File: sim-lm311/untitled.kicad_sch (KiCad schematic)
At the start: 6 parts, among them Q1 NMOS, Q2 NMOS, U4 L7805

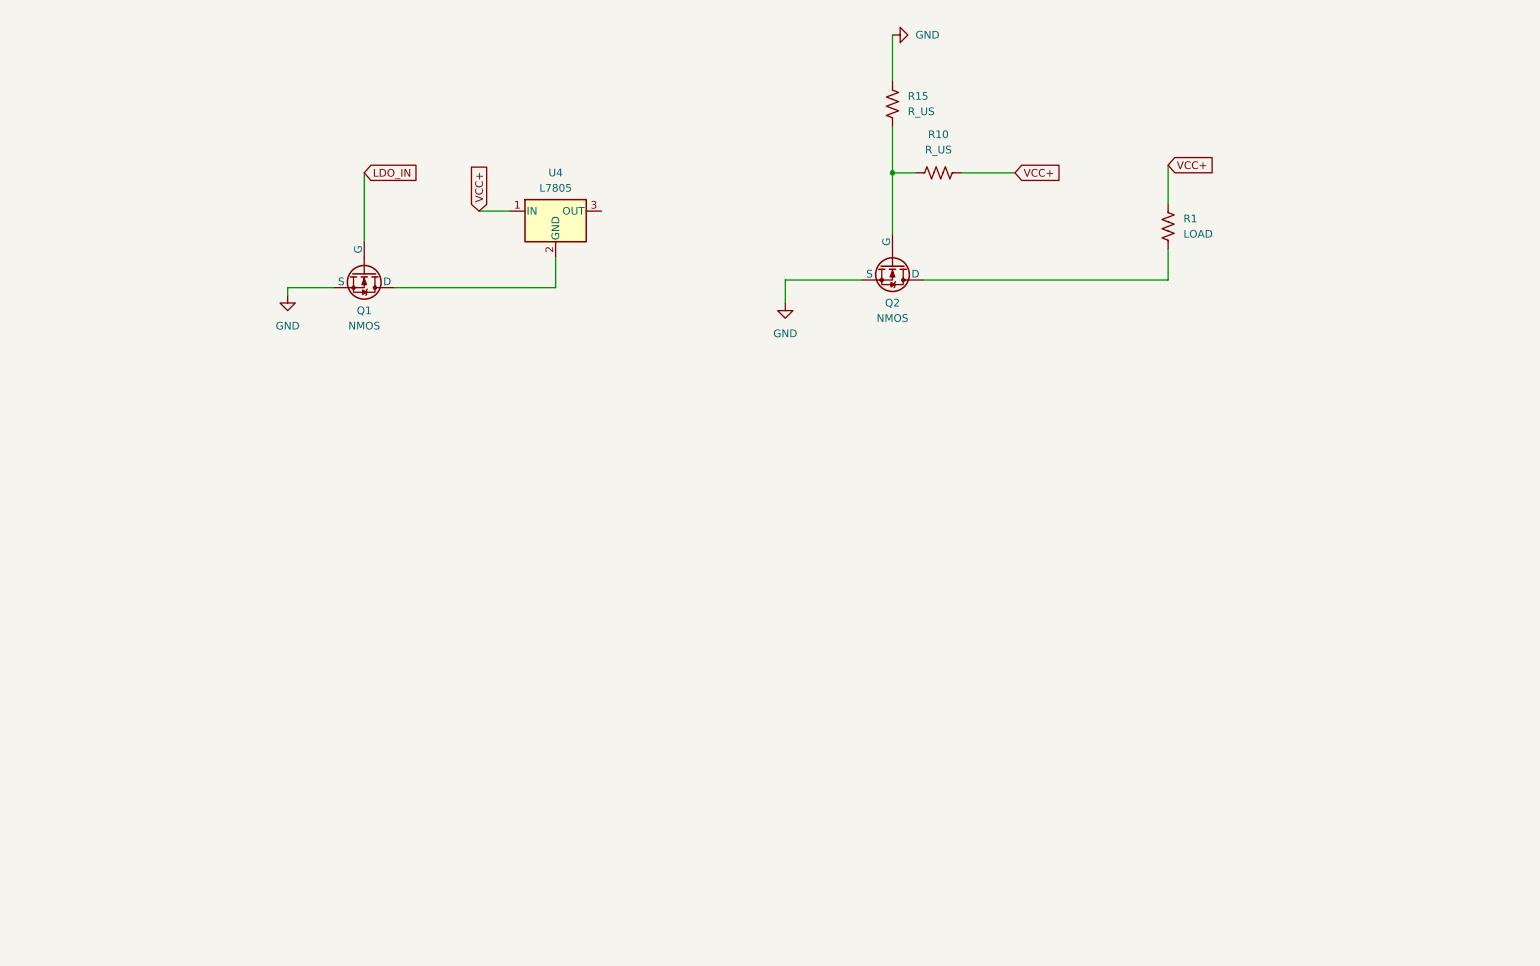
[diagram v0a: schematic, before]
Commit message: updated prototyping subcircuit under lm311
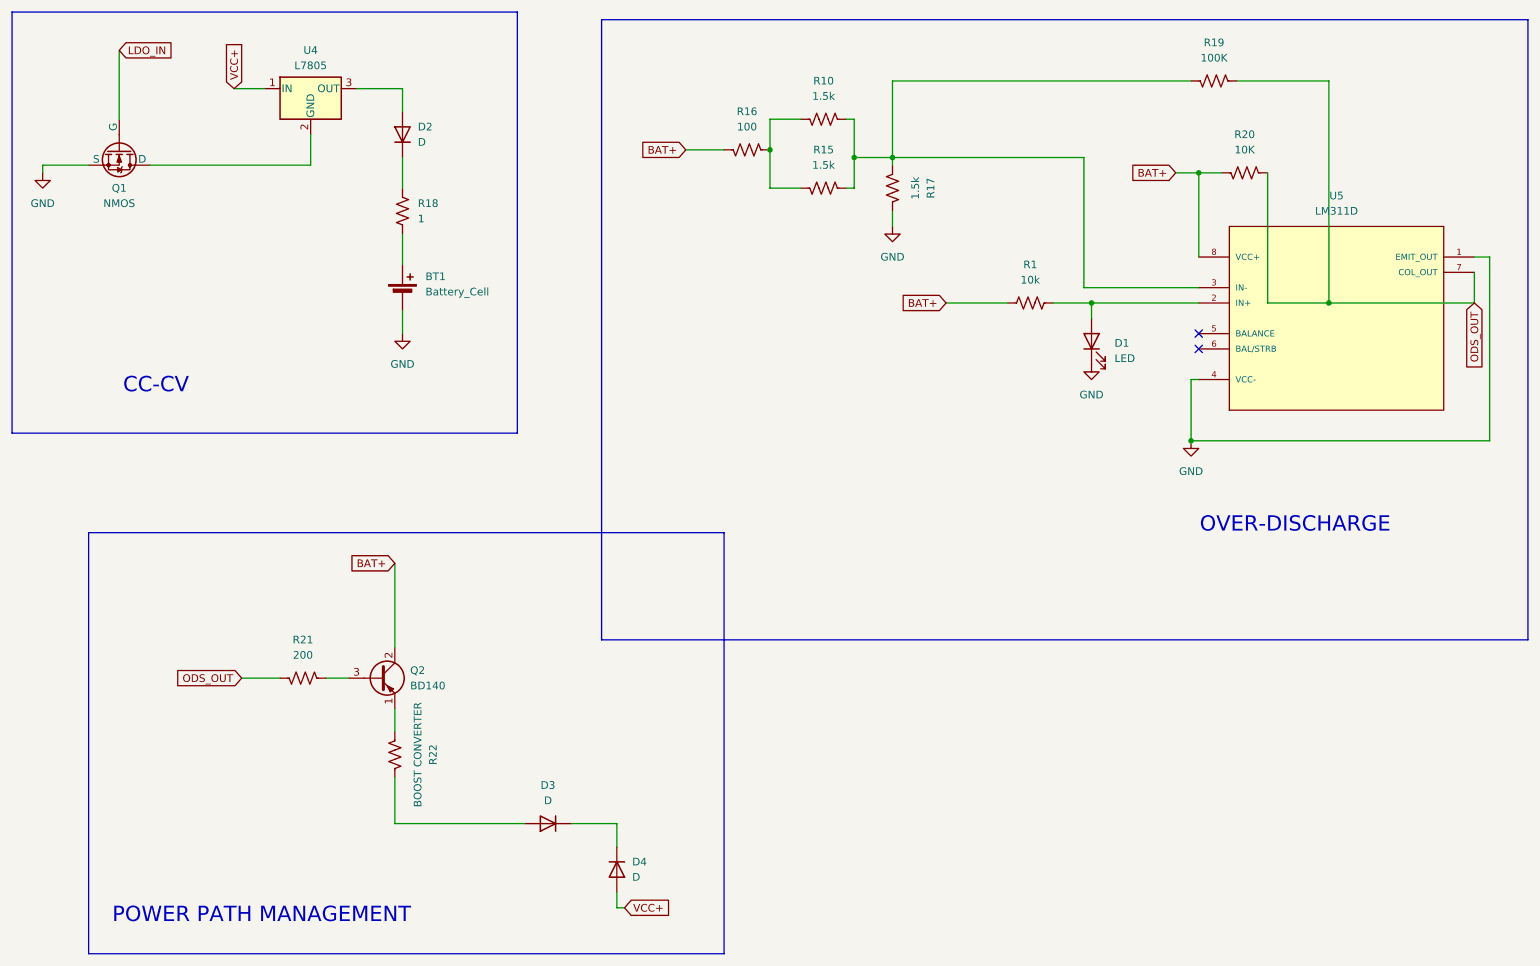
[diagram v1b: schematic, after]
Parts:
- removed Q2: NMOS, symbol Simulation_SPICE:NMOS
- added BT1: Battery_Cell, symbol Device:Battery_Cell
- added D1: LED, symbol Device:LED
- added D2, D3, D4: D, symbol Device:D
- added Q2: BD140, Package_TO_SOT_THT:TO-126-3_Vertical, symbol Transistor_BJT:BD140
- added R16: 100, symbol Device:R_US
- added R17: 1.5k, symbol Device:R_US
- added R18: 1, symbol Device:R_US
- added R19: 100K, symbol Device:R_US
- added R20: 10K, symbol Device:R_US
- added R21: 200, symbol Device:R_US
- added R22: BOOST CONVERTER, symbol Device:R_US
- added U5: LM311D, LM311D:SOIC127P600X175-8N, symbol LM311D:LM311D
- R1: value LOAD -> 10k
- R10, R15: value R_US -> 1.5k
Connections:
- net GND: now also BT1.2 (-), D1.1 (K), R17.1, U5.1 (EMIT_OUT), U5.4 (VCC-); no longer R15.2
- net VCC+: now also D4.2 (A); no longer R1.1, R10.2
- net at U4.3 (OUT): now also D2.2 (A)
- net at R10.1, R15.1: now also R17.2, R19.2, U5.3 (IN-)
- net at R1.2: now also D1.2 (A), U5.2 (IN+)
- new net: D2.1 (K), R18.1
- new net: BT1.1 (+), R18.2
- new net: R10.2, R15.2, R16.1
- new net: Q2.1 (E), R22.2
- new net: Q2.3 (B), R21.1
- new net: D3.2 (A), R22.1
- new net: D3.1 (K), D4.1 (K)
- new net BAT+: Q2.2 (C), R1.1, R16.2, R20.2, U5.8 (VCC+)
- new net ODS_OUT: R19.1, R20.1, R21.2, U5.7 (COL_OUT)
- no-connect marks 0 -> 2
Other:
- note added: "CC-CV"
- note added: "OVER-DISCHARGE"
- note added: "POWER PATH MANAGEMENT"
- moved on the sheet: Q1, U4
